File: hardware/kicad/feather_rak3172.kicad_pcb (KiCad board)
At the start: 2 copper layers, 51 x 23.1 mm, 51 parts, among them J1 Pin Header, J2 Pin Header, J3 USB_C_Receptacle_USB2.0, J4 915MHz SMA, J5 SWD, J6 JST-2PH, Q1 DMG341, SW1 RESET, SW2 BOOT, U1 RAK3172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

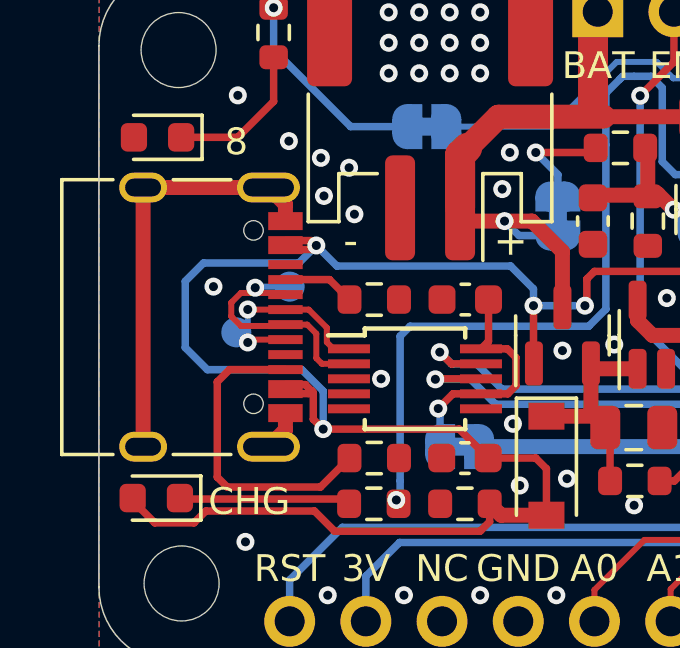
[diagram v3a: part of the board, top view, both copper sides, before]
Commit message: remove usb-c shield ground connection
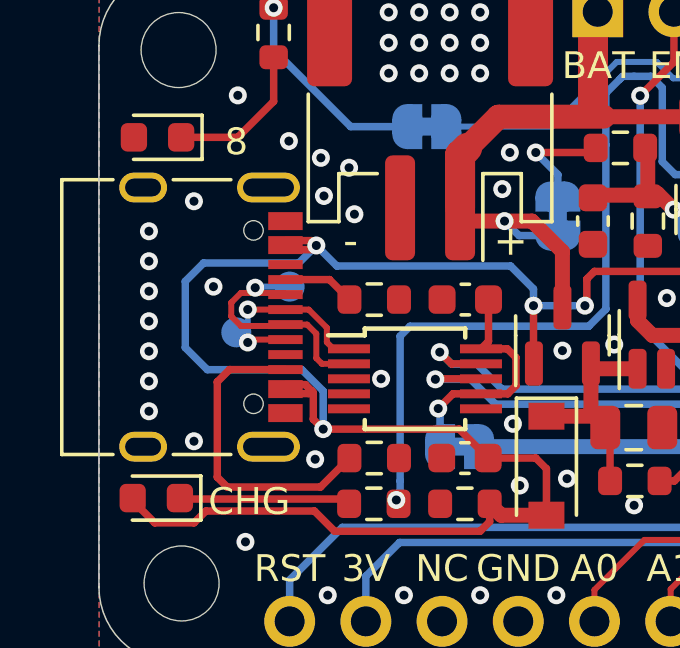
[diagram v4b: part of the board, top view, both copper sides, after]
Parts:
- D1: value RED -> BLUE
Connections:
- J3 pad S1: GND -> unconnected-(J3-PadS1)
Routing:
- net GND: track 16.6 -> 1.41 mm, vias 106 -> 116
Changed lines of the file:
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@@
   (title_block
     (title "Feather RAK3172")
-    (date "2023-01-24")
-    (rev "4.4")
+    (date "2023-02-06")
+    (rev "4.5")
     (company "Teapot Laboratories")
   )
@@
   (net 53 "Net-(JP2-Pad1)")
   (net 54 "Net-(JP4-Pad1)")
+  (net 55 "unconnected-(J3-PadS1)")
   (footprint "Inductor_SMD:L_0402_1005Metric" (layer "F.Cu")
     (at 162.306 99.845 -90)
@@
     (descr "Capacitor SMD 0603 (1608 Metric), square (rectangular) end terminal, IPC_7351 nominal, (Body size source: IPC-SM-782 page 76, https://www.pcb-3d.com/wordpress/wp-content/uploads/ipc-sm-782a_amendment_1_and_2.pdf), generated with kicad-footprint-generator")
     (tags "capacitor")
-    (property "Part Description" "Ceramic Capacitor 100nF 10% 10V X5R")
+    (property "Part Description" "Ceramic Capacitor 100nF 10% 10V X7R")
     (property "Sheetfile" "feather_rak3172.kicad_sch")
     (property "Sheetname" "")
@@
       (net 1 "GND") (pinfunction "GND") (pintype "passive"))
     (pad "S1" thru_hole oval (at -4.32 -3.105 270) (size 1 2.1) (drill oval 0.6 1.7) (layers *.Cu *.Mask)
-      (net 1 "GND") (pinfunction "SHIELD") (pintype "passive"))
+      (net 55 "unconnected-(J3-PadS1)") (pinfunction "SHIELD") (pintype "passive+no_connect"))
     (pad "S1" thru_hole oval (at 4.32 -3.105 270) (size 1 2.1) (drill oval 0.6 1.7) (layers *.Cu *.Mask)
-      (net 1 "GND") (pinfunction "SHIELD") (pintype "passive"))
+      (net 55 "unconnected-(J3-PadS1)") (pinfunction "SHIELD") (pintype "passive+no_connect"))
     (pad "S1" thru_hole oval (at -4.32 1.075 270) (size 1 1.6) (drill oval 0.6 1.2) (layers *.Cu *.Mask)
-      (net 1 "GND") (pinfunction "SHIELD") (pintype "passive"))
+      (net 55 "unconnected-(J3-PadS1)") (pinfunction "SHIELD") (pintype "passive+no_connect"))
     (pad "S1" thru_hole oval (at 4.32 1.075 270) (size 1 1.6) (drill oval 0.6 1.2) (layers *.Cu *.Mask)
-      (net 1 "GND") (pinfunction "SHIELD") (pintype "passive"))
+      (net 55 "unconnected-(J3-PadS1)") (pinfunction "SHIELD") (pintype "passive+no_connect"))
     (model "${TEAPOT_3DMODEL_DIR}/u262-161n-4bvc11.stp"
       (offset (xyz 0 -3.5 1.7))
@@
     (descr "Capacitor SMD 0603 (1608 Metric), square (rectangular) end terminal, IPC_7351 nominal, (Body size source: IPC-SM-782 page 76, https://www.pcb-3d.com/wordpress/wp-content/uploads/ipc-sm-782a_amendment_1_and_2.pdf), generated with kicad-footprint-generator")
     (tags "capacitor")
-    (property "Part Description" "Ceramic Capacitor 100nF 10% 10V X5R")
+    (property "Part Description" "Ceramic Capacitor 100nF 10% 10V X7R")
     (property "Sheetfile" "feather_rak3172.kicad_sch")
     (property "Sheetname" "")
@@
     (descr "Capacitor SMD 0603 (1608 Metric), square (rectangular) end terminal, IPC_7351 nominal, (Body size source: IPC-SM-782 page 76, https://www.pcb-3d.com/wordpress/wp-content/uploads/ipc-sm-782a_amendment_1_and_2.pdf), generated with kicad-footprint-generator")
     (tags "capacitor")
-    (property "Part Description" "Ceramic Capacitor 100nF 10% 10V X5R")
+    (property "Part Description" "Ceramic Capacitor 100nF 10% 10V X7R")
     (property "Sheetfile" "feather_rak3172.kicad_sch")
     (property "Sheetname" "")
@@
     (descr "Capacitor SMD 0603 (1608 Metric), square (rectangular) end terminal, IPC_7351 nominal, (Body size source: IPC-SM-782 page 76, https://www.pcb-3d.com/wordpress/wp-content/uploads/ipc-sm-782a_amendment_1_and_2.pdf), generated with kicad-footprint-generator")
     (tags "capacitor")
-    (property "Part Description" "Ceramic Capacitor 100nF 10% 10V X5R")
+    (property "Part Description" "Ceramic Capacitor 100nF 10% 10V X7R")
     (property "Sheetfile" "feather_rak3172.kicad_sch")
     (property "Sheetname" "")
@@
       (effects (font (size 0.5 0.5) (thickness 0.125)))
     )
-    (fp_text value "RED" (at -0.0855 0.1035) (layer "F.Fab")
+    (fp_text value "BLUE" (at -0.0855 0.1035) (layer "F.Fab")
       (effects (font (size 0.5 0.5) (thickness 0.125)))
     )
@@
     (effects (font (size 0.89408 0.89408) (thickness 0.15)))
   )
-  (segment (start 123.05 99.012) (end 123.05 98.607) (width 0.5) (layer "F.Cu") (net 1))
-  (segment (start 122.485 98.042) (end 118.305 98.042) (width 0.5) (layer "F.Cu") (net 1))
-  (segment (start 123.05 105.712) (end 123.05 106.117) (width 0.5) (layer "F.Cu") (net 1))
-  (segment (start 123.05 98.607) (end 122.485 98.042) (width 0.5) (layer "F.Cu") (net 1))
   (segment (start 151.8196 109.7366) (end 151.8196 108.3348) (width 0.5) (layer "F.Cu") (net 1))
-  (segment (start 118.305 106.682) (end 118.305 98.042) (width 0.5) (layer "F.Cu") (net 1))
   (segment (start 151.8196 108.3348) (end 151.8158 108.331) (width 0.5) (layer "F.Cu") (net 1))
-  (segment (start 123.05 106.117) (end 122.485 106.682) (width 0.5) (layer "F.Cu") (net 1))
   (via (at 160.1216 110.1344) (size 0.6) (drill 0.3) (layers "F.Cu" "B.Cu") (free) (net 1))
   (via (at 130.5306 96.8756) (size 0.6) (drill 0.3) (layers "F.Cu" "B.Cu") (free) (net 1))
@@
   (via (at 146.177 102.235) (size 0.6) (drill 0.3) (layers "F.Cu" "B.Cu") (free) (net 1))
   (via (at 142.367 109.0676) (size 0.6) (drill 0.3) (layers "F.Cu" "B.Cu") (free) (net 1))
+  (via (at 124.04 107.1) (size 0.6) (drill 0.3) (layers "F.Cu" "B.Cu") (free) (net 1))
   (via (at 164.0078 96.4184) (size 0.6) (drill 0.3) (layers "F.Cu" "B.Cu") (free) (net 1))
   (via (at 128.524 94.234) (size 0.6) (drill 0.3) (layers "F.Cu" "B.Cu") (free) (net 1))
   (via (at 165.1762 101.1682) (size 0.6) (drill 0.3) (layers "F.Cu" "B.Cu") (free) (net 1))
+  (via (at 120 98.5) (size 0.6) (drill 0.3) (layers "F.Cu" "B.Cu") (free) (net 1))
   (via (at 123.1646 96.4946) (size 0.6) (drill 0.3) (layers "F.Cu" "B.Cu") (free) (net 1))
   (via (at 132.2832 103.4796) (size 0.6) (drill 0.3) (layers "F.Cu" "B.Cu") (free) (net 1))
@@
   (via (at 160.1216 109.093) (size 0.6) (drill 0.3) (layers "F.Cu" "B.Cu") (free) (net 1))
   (via (at 125.1712 97.3836) (size 0.6) (drill 0.3) (layers "F.Cu" "B.Cu") (free) (net 1))
+  (via (at 118.5 100.5) (size 0.6) (drill 0.3) (layers "F.Cu" "B.Cu") (free) (net 1))
   (via (at 163.449 97.9932) (size 0.6) (drill 0.3) (layers "F.Cu" "B.Cu") (free) (net 1))
   (via (at 143.891 100.203) (size 0.6) (drill 0.3) (layers "F.Cu" "B.Cu") (free) (net 1))
@@
   (via (at 166.4462 96.9264) (size 0.6) (drill 0.3) (layers "F.Cu" "B.Cu") (free) (net 1))
   (via (at 126.492 93.218) (size 0.6) (drill 0.3) (layers "F.Cu" "B.Cu") (free) (net 1))
+  (via (at 120 106.5) (size 0.6) (drill 0.3) (layers "F.Cu" "B.Cu") (free) (net 1))
   (via (at 166.0906 103.2256) (size 0.6) (drill 0.3) (layers "F.Cu" "B.Cu") (free) (net 1))
   (via (at 127 111.633) (size 0.6) (drill 0.3) (layers "F.Cu" "B.Cu") (free) (net 1))
@@
   (via (at 134.0104 103.2764) (size 0.6) (drill 0.3) (layers "F.Cu" "B.Cu") (free) (net 1))
   (via (at 137.287 92.964) (size 0.6) (drill 0.3) (layers "F.Cu" "B.Cu") (free) (net 1))
+  (via (at 118.5 104.5) (size 0.6) (drill 0.3) (layers "F.Cu" "B.Cu") (free) (net 1))
   (via (at 164.7698 107.1372) (size 0.6) (drill 0.3) (layers "F.Cu" "B.Cu") (free) (net 1))
   (via (at 161.5948 107.315) (size 0.6) (drill 0.3) (layers "F.Cu" "B.Cu") (free) (net 1))
@@
   (via (at 166.6494 95.6818) (size 0.6) (drill 0.3) (layers "F.Cu" "B.Cu") (free) (net 1))
   (via (at 164.4142 97.9678) (size 0.6) (drill 0.3) (layers "F.Cu" "B.Cu") (free) (net 1))
+  (via (at 118.5 103.5) (size 0.6) (drill 0.3) (layers "F.Cu" "B.Cu") (free) (net 1))
   (via (at 161.4424 108.5342) (size 0.6) (drill 0.3) (layers "F.Cu" "B.Cu") (free) (net 1))
   (via (at 124.46 111.633) (size 0.6) (drill 0.3) (layers "F.Cu" "B.Cu") (free) (net 1))
@@
   (via (at 142.9512 98.425) (size 0.6) (drill 0.3) (layers "F.Cu" "B.Cu") (free) (net 1))
   (via (at 163.449 95.25) (size 0.6) (drill 0.3) (layers "F.Cu" "B.Cu") (free) (net 1))
+  (via (at 118.5 102.5) (size 0.6) (drill 0.3) (layers "F.Cu" "B.Cu") (free) (net 1))
   (via (at 134.6708 108.6358) (size 0.6) (drill 0.3) (layers "F.Cu" "B.Cu") (free) (net 1))
   (via (at 129.54 93.218) (size 0.6) (drill 0.3) (layers "F.Cu" "B.Cu") (free) (net 1))
+  (via (at 118.5 99.5) (size 0.6) (drill 0.3) (layers "F.Cu" "B.Cu") (free) (net 1))
   (via (at 165.1762 103.505) (size 0.6) (drill 0.3) (layers "F.Cu" "B.Cu") (free) (net 1))
   (via (at 144.272 101.092) (size 0.6) (drill 0.3) (layers "F.Cu" "B.Cu") (free) (net 1))
@@
   (via (at 161.5694 102.5144) (size 0.6) (drill 0.3) (layers "F.Cu" "B.Cu") (free) (net 1))
   (via (at 161.6456 105.0798) (size 0.6) (drill 0.3) (layers "F.Cu" "B.Cu") (free) (net 1))
+  (via (at 118.5 105.5) (size 0.6) (drill 0.3) (layers "F.Cu" "B.Cu") (free) (net 1))
   (via (at 162.1028 96.139) (size 0.6) (drill 0.3) (layers "F.Cu" "B.Cu") (free) (net 1))
   (via (at 132.08 111.633) (size 0.6) (drill 0.3) (layers "F.Cu" "B.Cu") (free) (net 1))
@@
   (via (at 165.608 98.044) (size 0.6) (drill 0.3) (layers "F.Cu" "B.Cu") (free) (net 1))
   (via (at 140.7668 96.0882) (size 0.6) (drill 0.3) (layers "F.Cu" "B.Cu") (free) (net 1))
+  (via (at 118.5 101.5) (size 0.6) (drill 0.3) (layers "F.Cu" "B.Cu") (free) (net 1))
   (via (at 166.8272 98.1202) (size 0.6) (drill 0.3) (layers "F.Cu" "B.Cu") (free) (net 1))
   (via (at 162.1282 103.0478) (size 0.6) (drill 0.3) (layers "F.Cu" "B.Cu") (free) (net 1))

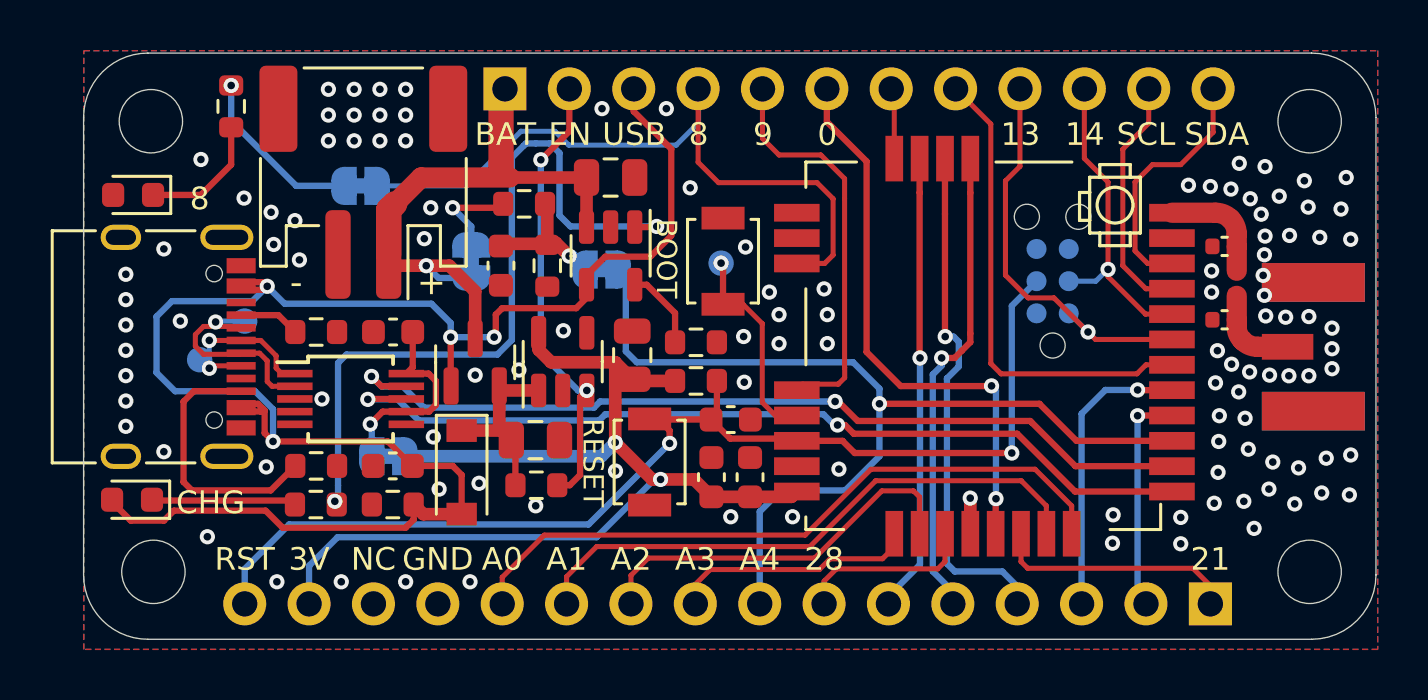
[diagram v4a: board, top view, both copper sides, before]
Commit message: move capacitor closer to charger chip
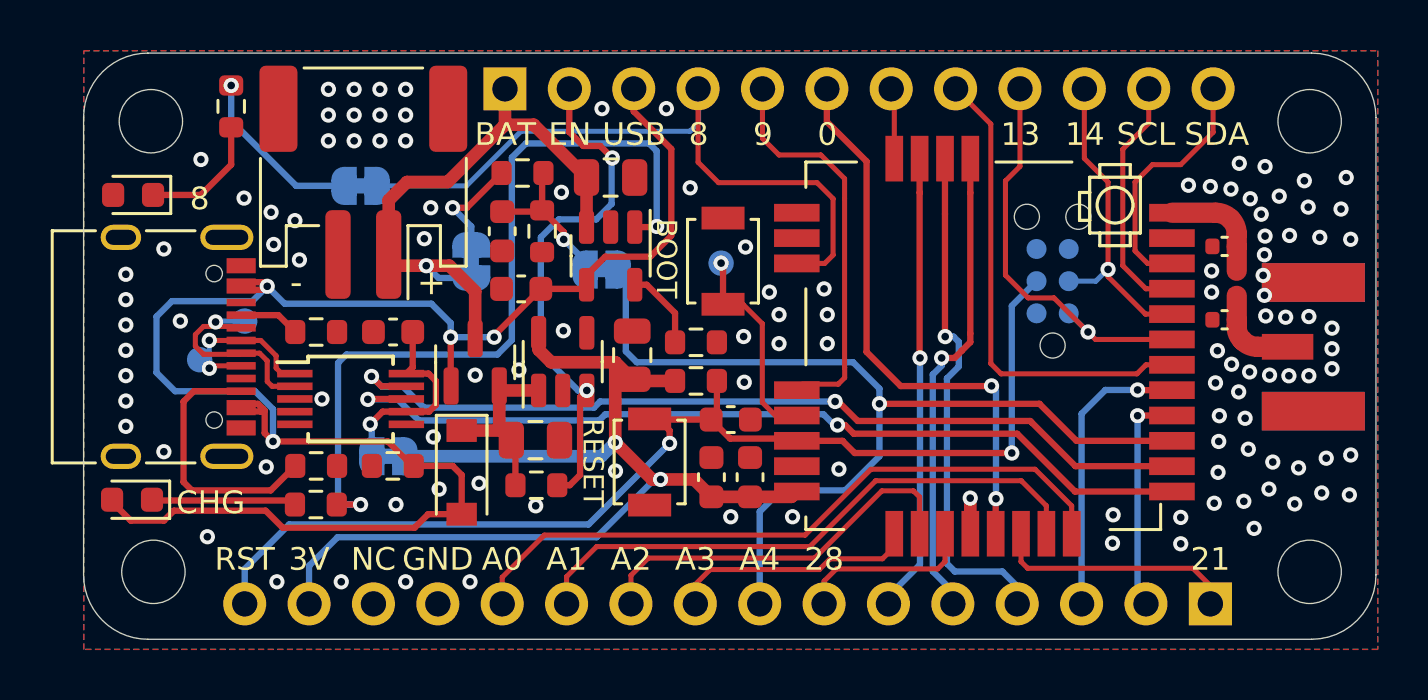
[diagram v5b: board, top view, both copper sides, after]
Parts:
- moved C6 8.63 mm to (134.1, 100.1)
- moved R7 1.52 mm to (129.0, 107.1)
- moved R10 1.37 mm to (134.9, 97.8)
- moved C11 1.36 mm to (133.3, 97.8)
- moved R9 1.22 mm to (134.2, 95.5)
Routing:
- net /EN: track 17.6 -> 20.3 mm
- net Net-(R6-Pad1): track 29.3 -> 31.6 mm
- net VBUS: track 72.2 -> 70.8 mm
- net Net-(C11-Pad1): track 5.31 -> 6.13 mm
- net Net-(JP4-Pad1): track 3.75 -> 4.27 mm
- net GND: vias 116 -> 118

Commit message: revision 5
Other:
- board text added: "Rev 5"
- board text removed: "Rev 4.4"
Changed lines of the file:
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@@
     (title "Feather RAK3172")
     (date "2023-02-06")
-    (rev "4.6")
+    (rev "5")
     (company "Teapot Laboratories")
   )
@@
     (effects (font (size 0.89408 0.89408) (thickness 0.15)) (justify mirror))
   )
-  (gr_text "Rev 4.4" (at 128.524 104.648) (layer "B.SilkS")
+  (gr_text "Rev 5" (at 128.524 104.648) (layer "B.SilkS")
     (effects (font (size 0.8 0.8) (thickness 0.1)) (justify mirror))
   )

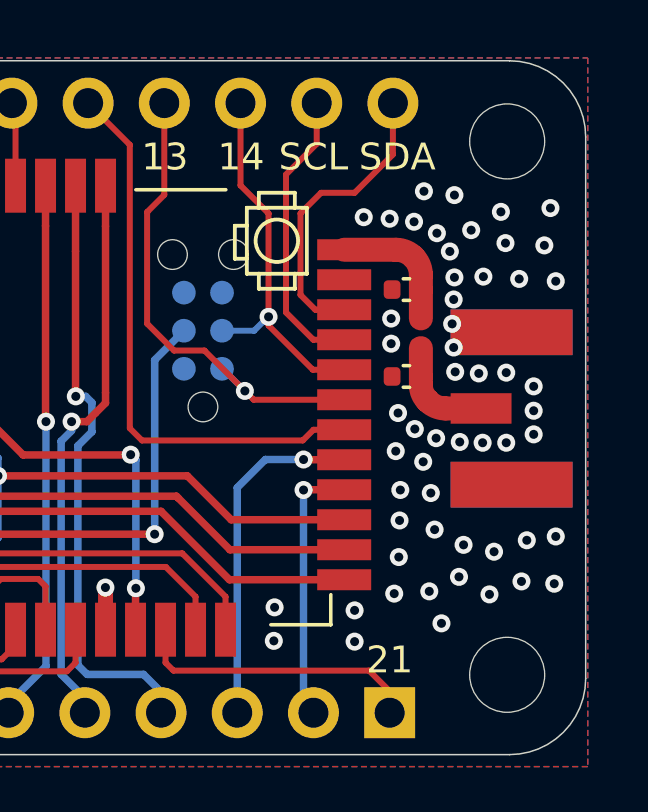
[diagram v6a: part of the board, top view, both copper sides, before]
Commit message: remove matching circuit, trace too short
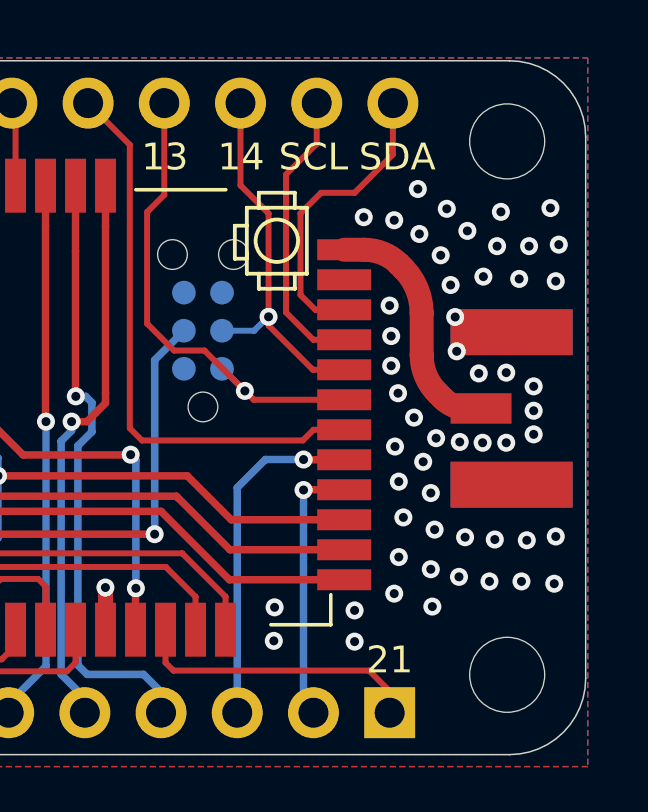
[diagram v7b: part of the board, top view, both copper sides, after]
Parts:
- removed C2, C5: ? F, Capacitor_SMD:C_0402_1005Metric
- removed L1: ? H, Inductor_SMD:L_0402_1005Metric
- C6: value 10nF -> 10uF
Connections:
- J4 pad 1: Net-(C5-Pad2) -> /RF
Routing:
- net /RF: track 4.45 -> 8.20 mm
- net Net-(C5-Pad2): track 3.62 -> 0.00 mm
- net GND: vias 118 -> 117
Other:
- board text added: "Rev 6"
- board text removed: "Rev 5"

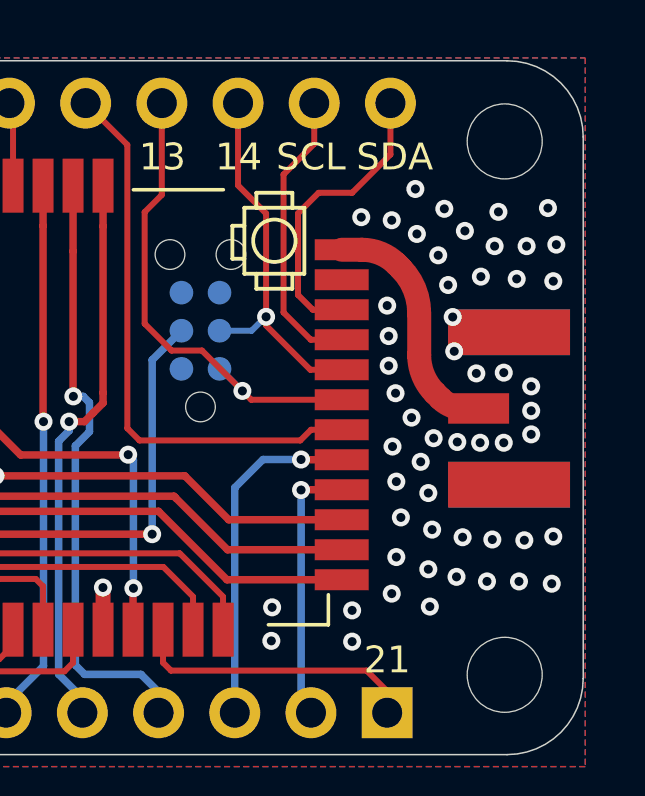
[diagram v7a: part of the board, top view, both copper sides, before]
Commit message: re-add matching circuit, improve rf trace angle
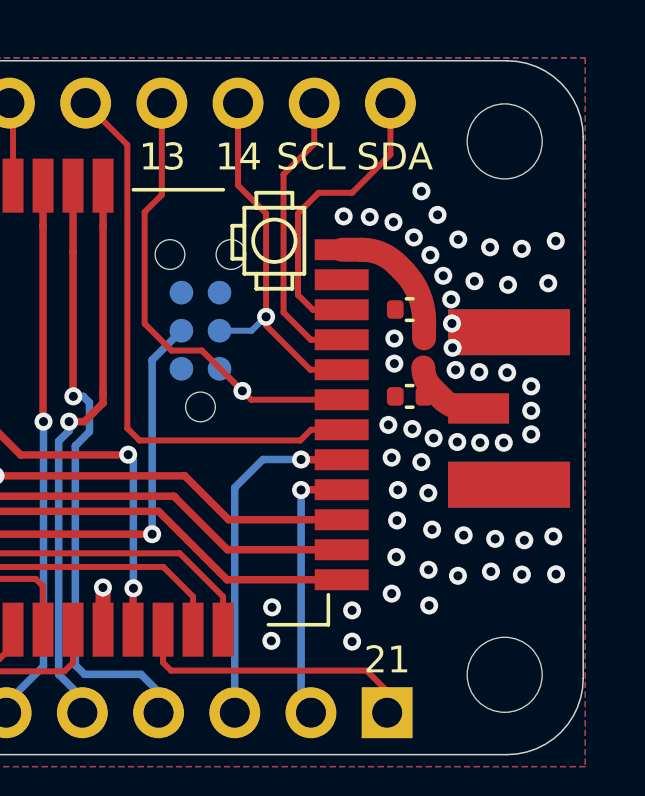
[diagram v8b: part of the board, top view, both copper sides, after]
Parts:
- added C2: ? F, Capacitor_SMD:C_0402_1005Metric, F.Cu at (162.0, 99.1)
- added C5: ? F, Capacitor_SMD:C_0402_1005Metric, F.Cu at (162.0, 102.0)
- added L1: ? H, Inductor_SMD:L_0402_1005Metric, F.Cu at (162.5, 100.5)
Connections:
- J4 pad 1: /RF -> Net-(C5-Pad2)
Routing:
- net /RF: track 8.20 -> 4.77 mm
- net Net-(C5-Pad2): track 0.00 -> 2.55 mm
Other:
- board text added: "Rev 7"
- board text removed: "Rev 6"
